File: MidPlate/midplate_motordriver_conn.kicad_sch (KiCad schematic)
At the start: 18 parts, among them J1 Conn_01x06, J2 Conn_02x20_Odd_Even

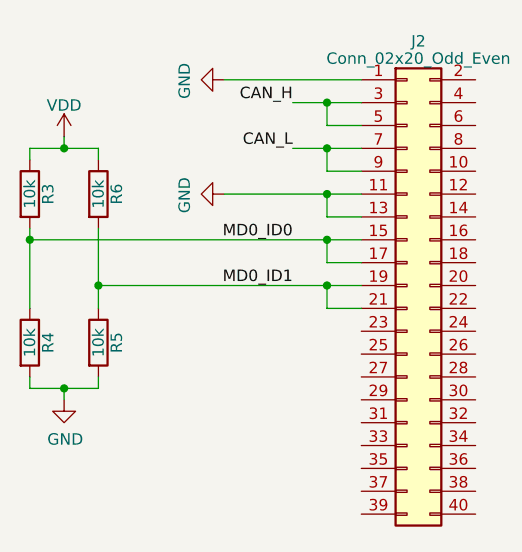
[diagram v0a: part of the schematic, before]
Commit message: update to power board and midplate schematics
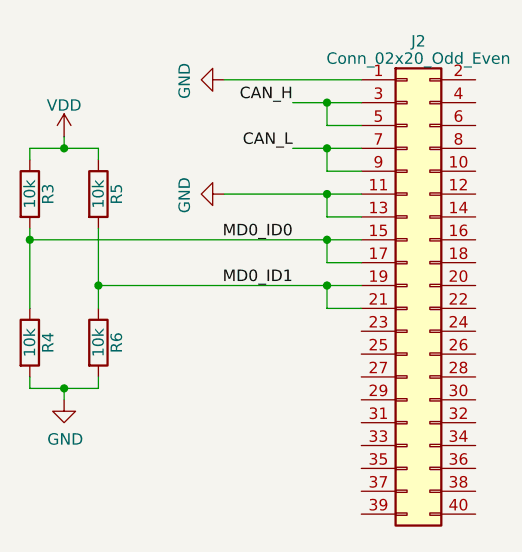
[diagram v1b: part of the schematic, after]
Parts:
- renumbered R6 to R5, R5 to R6

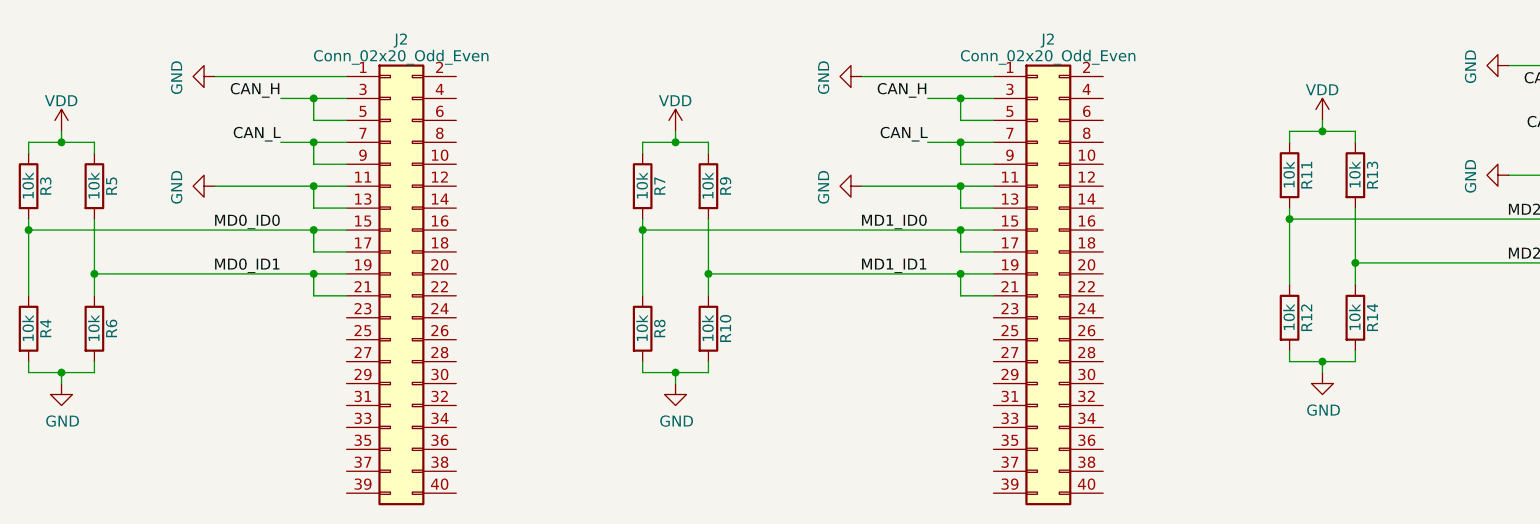
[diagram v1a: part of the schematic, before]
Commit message: added switch and fuse
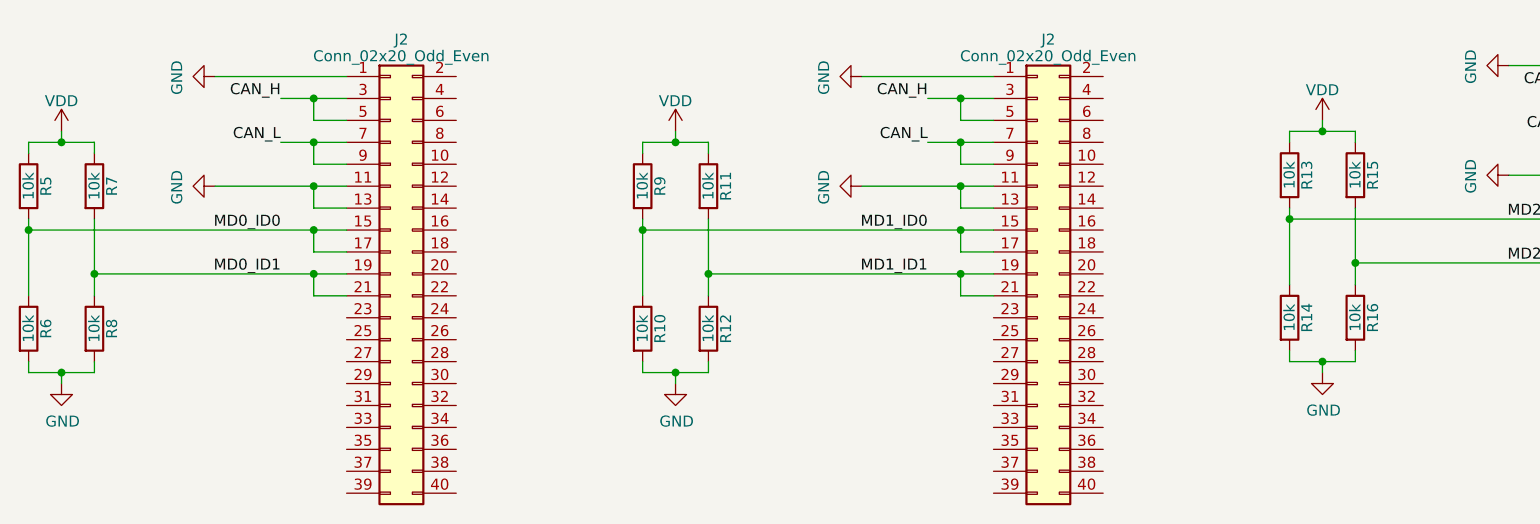
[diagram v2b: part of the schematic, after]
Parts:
- renumbered R8 to R10, R9 to R11, R10 to R12, R11 to R13, R12 to R14, R13 to R15, R14 to R16, R3 to R5, R4 to R6, R5 to R7, R6 to R8, R7 to R9

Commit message: powerboard HV powerpillars + midplate
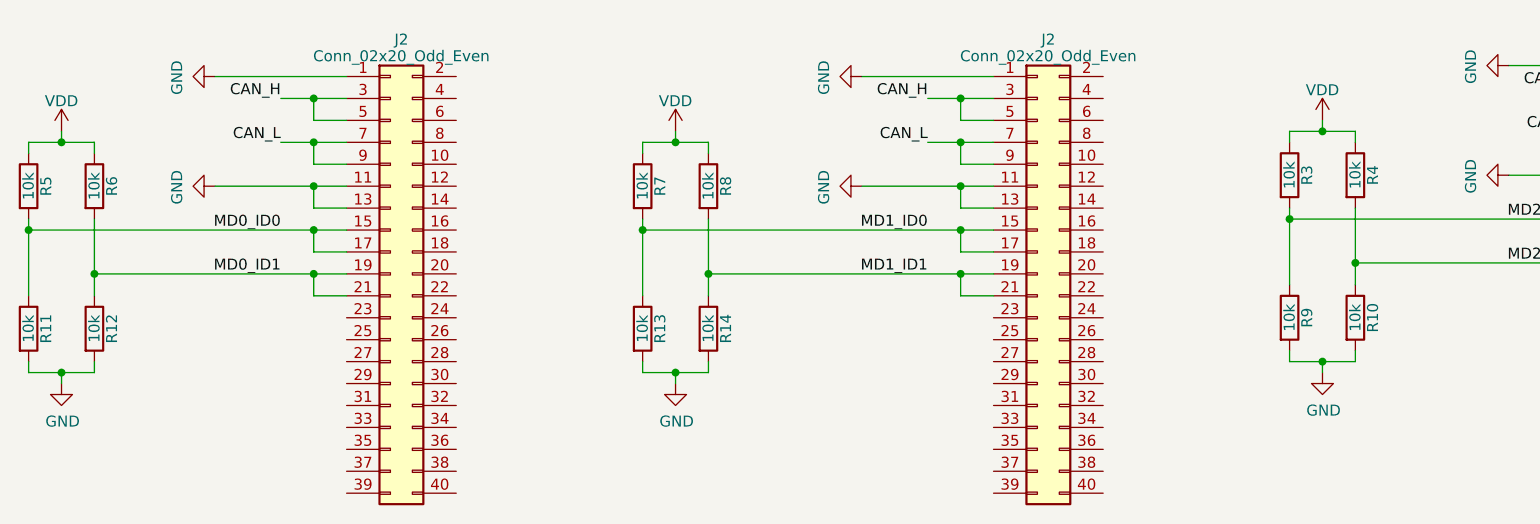
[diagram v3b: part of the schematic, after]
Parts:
- renumbered R16 to R10, R6 to R11, R8 to R12, R10 to R13, R12 to R14, R13 to R3, R15 to R4, R7 to R6, R9 to R7, R11 to R8, R14 to R9

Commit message: midplate mods
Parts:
- added J13: JST_BM04B-GHS-TBT, bots:JST_BM04B-GHS-TBT, symbol bots:JST_BM04B-GHS-TBT
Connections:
- net GND: now also J13.2
- new net CAN+: J13.4
- new net CAN-: J13.3
- new net VCC: J13.1
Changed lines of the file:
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@@
+    (stroke (width 0) (type default))
+  )
+  (wire (pts (xy 68.58 163.83) (xy 68.58 171.45))
     (stroke (width 0) (type default))
   )
@@
     (stroke (width 0) (type default))
   )
+  (wire (pts (xy 86.36 167.64) (xy 71.12 167.64))
+    (stroke (width 0) (type default))
+  )
   (wire (pts (xy 189.23 74.93) (xy 189.23 73.66))
     (stroke (width 0) (type default))
@@
     (stroke (width 0) (type default))
   )
+  (wire (pts (xy 86.36 167.64) (xy 86.36 179.07))
+    (stroke (width 0) (type default))
+  )
   (wire (pts (xy 71.12 123.19) (xy 88.9 123.19))
     (stroke (width 0) (type default))
@@
     (stroke (width 0) (type default))
   )
+  (wire (pts (xy 66.04 163.83) (xy 66.04 171.45))
+    (stroke (width 0) (type default))
+  )
   (wire (pts (xy 193.04 46.99) (xy 193.04 48.26))
     (stroke (width 0) (type default))
@@
     (stroke (width 0) (type default))
   )
+  (wire (pts (xy 60.96 171.45) (xy 60.96 180.34))
+    (stroke (width 0) (type default))
+  )
   (wire (pts (xy 147.32 50.8) (xy 147.32 48.26))
     (stroke (width 0) (type default))
@@
     (stroke (width 0) (type default))
   )
+  (wire (pts (xy 60.96 171.45) (xy 66.04 171.45))
+    (stroke (width 0) (type default))
+  )
   (wire (pts (xy 68.58 48.26) (xy 72.39 48.26))
     (stroke (width 0) (type default))
@@
     (stroke (width 0) (type default))
   )
+  (wire (pts (xy 68.58 171.45) (xy 74.93 171.45))
+    (stroke (width 0) (type default))
+  )
   (wire (pts (xy 143.51 48.26) (xy 147.32 48.26))
     (stroke (width 0) (type default))
@@
     (stroke (width 0) (type default))
   )
+  (wire (pts (xy 49.53 168.91) (xy 49.53 179.07))
+    (stroke (width 0) (type default))
+  )
+  (wire (pts (xy 74.93 171.45) (xy 74.93 179.07))
+    (stroke (width 0) (type default))
+  )
   (wire (pts (xy 88.9 118.11) (xy 88.9 115.57))
     (stroke (width 0) (type default))
@@
     (stroke (width 0) (type default))
   )
+  (wire (pts (xy 63.5 168.91) (xy 63.5 163.83))
+    (stroke (width 0) (type default))
+  )
   (wire (pts (xy 238.76 114.3) (xy 238.76 111.76))
     (stroke (width 0) (type default))
@@
     (stroke (width 0) (type default))
   )
+  (wire (pts (xy 49.53 168.91) (xy 63.5 168.91))
+    (stroke (width 0) (type default))
+  )
   (wire (pts (xy 88.9 123.19) (xy 88.9 125.73))
     (stroke (width 0) (type default))
@@
   )
   (wire (pts (xy 43.18 76.2) (xy 43.18 74.93))
+    (stroke (width 0) (type default))
+  )
+  (wire (pts (xy 71.12 167.64) (xy 71.12 163.83))
     (stroke (width 0) (type default))
   )
@@
   (label "MD2_ID1" (at 218.44 62.23 180) (fields_autoplaced)
     (effects (font (size 1.27 1.27)) (justify right bottom))
+  )
+  (global_label "CAN+" (shape input) (at 86.36 179.07 270) (fields_autoplaced)
+    (effects (font (size 1.27 1.27)) (justify right))
+    (property "Intersheetrefs" "${INTERSHEET_REFS}" (at 86.36 187.3167 90)
+      (effects (font (size 1.27 1.27)) (justify right) hide)
+    )
+  )
+  (global_label "CAN-" (shape input) (at 74.93 179.07 270) (fields_autoplaced)
+    (effects (font (size 1.27 1.27)) (justify right))
+    (property "Intersheetrefs" "${INTERSHEET_REFS}" (at 74.93 187.3167 90)
+      (effects (font (size 1.27 1.27)) (justify right) hide)
+    )
   )
   (symbol (lib_id "Connector_Generic:Conn_02x20_Odd_Even") (at 231.14 62.23 0) (unit 1)
@@
     )
   )
+  (symbol (lib_id "bots:JST_BM04B-GHS-TBT") (at 66.04 158.75 90) (unit 1)
+    (in_bom yes) (on_board yes) (dnp no)
+    (property "Reference" "J13" (at 64.77 149.86 90)
+      (effects (font (size 1.27 1.27)) (justify right))
+    )
+    (property "Value" "JST_BM04B-GHS-TBT" (at 71.12 160.02 90)
+      (effects (font (size 1.27 1.27)) (justify right))
+    )
+    (property "Footprint" "bots:JST_BM04B-GHS-TBT" (at 66.04 158.75 0)
+      (effects (font (size 1.27 1.27)) (justify bottom) hide)
+    )
+    (property "Datasheet" "" (at 66.04 158.75 0)
+      (effects (font (size 1.27 1.27)) hide)
+    )
+    (property "MPN" "BM04B-GHS-TBT" (at 66.04 158.75 0)
+      (effects (font (size 1.27 1.27)) (justify bottom) hide)
+    )
+    (property "Manufacturer" "JST Sales America Inc." (at 66.04 158.75 0)
+      (effects (font (size 1.27 1.27)) (justify bottom) hide)
+    )
+    (property "Price" "0.31" (at 66.04 158.75 0)
+      (effects (font (size 1.27 1.27)) hide)
+    )
+    (property "JLC" "" (at 66.04 158.75 0)
+      (effects (font (size 1.27 1.27)) hide)
+    )
+    (property "LCSC" "" (at 66.04 158.75 0)
+      (effects (font (size 1.27 1.27)) hide)
+    )
+    (pin "1")
+    (pin "2")
+    (pin "3")
+    (pin "4")
+    (pin "S1")
+    (pin "S2")
+    (instances
+      (project "midplate"
+        (path "/69058343-dac8-421b-a3f6-e069eb1ba8ae/ee29c8c0-427f-4977-aab8-03cf64edc230"
+          (reference "J13") (unit 1)
+        )
+      )
+    )
+  )
   (symbol (lib_id "power:GND") (at 210.82 39.37 270) (unit 1)
     (in_bom yes) (on_board yes) (dnp no)
@@
         (path "/69058343-dac8-421b-a3f6-e069eb1ba8ae/ee29c8c0-427f-4977-aab8-03cf64edc230"
           (reference "R14") (unit 1)
+        )
+      )
+    )
+  )
+  (symbol (lib_id "power:GND") (at 60.96 180.34 0) (unit 1)
+    (in_bom yes) (on_board yes) (dnp no) (fields_autoplaced)
+    (property "Reference" "#PWR037" (at 60.96 186.69 0)
+      (effects (font (size 1.27 1.27)) hide)
+    )
+    (property "Value" "GND" (at 60.96 185.42 0)
+      (effects (font (size 1.27 1.27)))
+    )
+    (property "Footprint" "" (at 60.96 180.34 0)
+      (effects (font (size 1.27 1.27)) hide)
+    )
+    (property "Datasheet" "" (at 60.96 180.34 0)
+      (effects (font (size 1.27 1.27)) hide)
+    )
+    (pin "1")
+    (instances
+      (project "midplate"
+        (path "/69058343-dac8-421b-a3f6-e069eb1ba8ae/ab54f000-c596-4ae0-81be-92723dd47fdf"
+          (reference "#PWR037") (unit 1)
+        )
+        (path "/69058343-dac8-421b-a3f6-e069eb1ba8ae/5699b499-0901-4542-927f-3a0270375bb5"
+          (reference "#PWR05") (unit 1)
+        )
+        (path "/69058343-dac8-421b-a3f6-e069eb1ba8ae/ee29c8c0-427f-4977-aab8-03cf64edc230"
+          (reference "#PWR027") (unit 1)
         )
       )
@@
         )
       )
+    )
+  )
+  (symbol (lib_id "power:VCC") (at 49.53 179.07 180) (unit 1)
+    (in_bom yes) (on_board yes) (dnp no) (fields_autoplaced)
+    (property "Reference" "#PWR04" (at 49.53 175.26 0)
+      (effects (font (size 1.27 1.27)) hide)
+    )
+    (property "Value" "VCC" (at 49.53 184.15 0)
+      (effects (font (size 1.27 1.27)))
+    )
+    (property "Footprint" "" (at 49.53 179.07 0)
+      (effects (font (size 1.27 1.27)) hide)
+    )
+    (property "Datasheet" "" (at 49.53 179.07 0)
+      (effects (font (size 1.27 1.27)) hide)
+    )
+    (pin "1")
+    (instances
+      (project "midplate"
+        (path "/69058343-dac8-421b-a3f6-e069eb1ba8ae/5699b499-0901-4542-927f-3a0270375bb5"
+          (reference "#PWR04") (unit 1)
+        )
+        (path "/69058343-dac8-421b-a3f6-e069eb1ba8ae/ee29c8c0-427f-4977-aab8-03cf64edc230"
+          (reference "#PWR026") (unit 1)
+        )
+      )
